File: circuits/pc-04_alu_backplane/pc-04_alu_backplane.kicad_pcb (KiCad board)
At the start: 2 copper layers, 99.1 x 99.1 mm, 16 parts, among them U1 74HC273, U2 74HC244, U3 74HC244, U4 74HC138, U5 4081, U6 4011, U7 4071, U8 74HC74, U9 4011

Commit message: Kicad upgrade to 9.0
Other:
- board text added: "ALU BACKPLANE PC-04 (REV. A)"
- board text removed: "ALU BACKPLANE PC-03 (REV. A)"

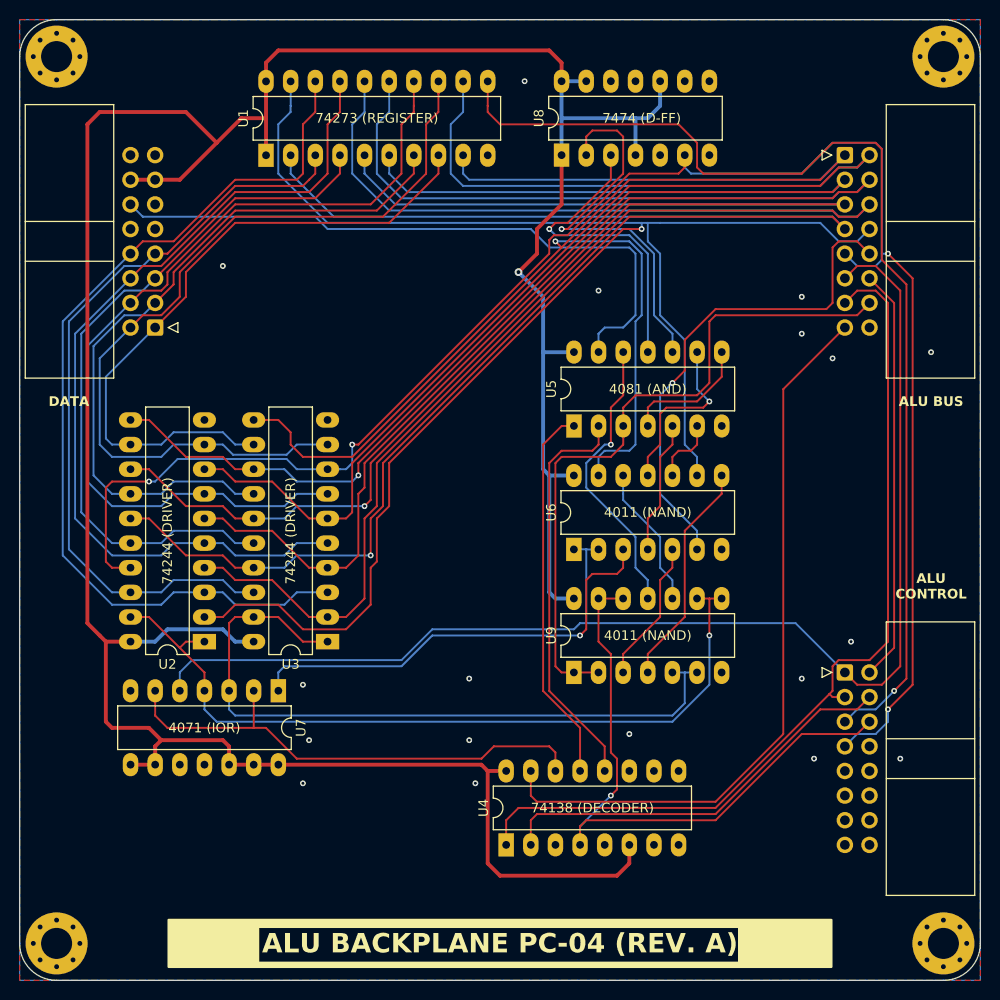
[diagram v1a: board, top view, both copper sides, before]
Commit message: pc-04: add missing pull-up resistors
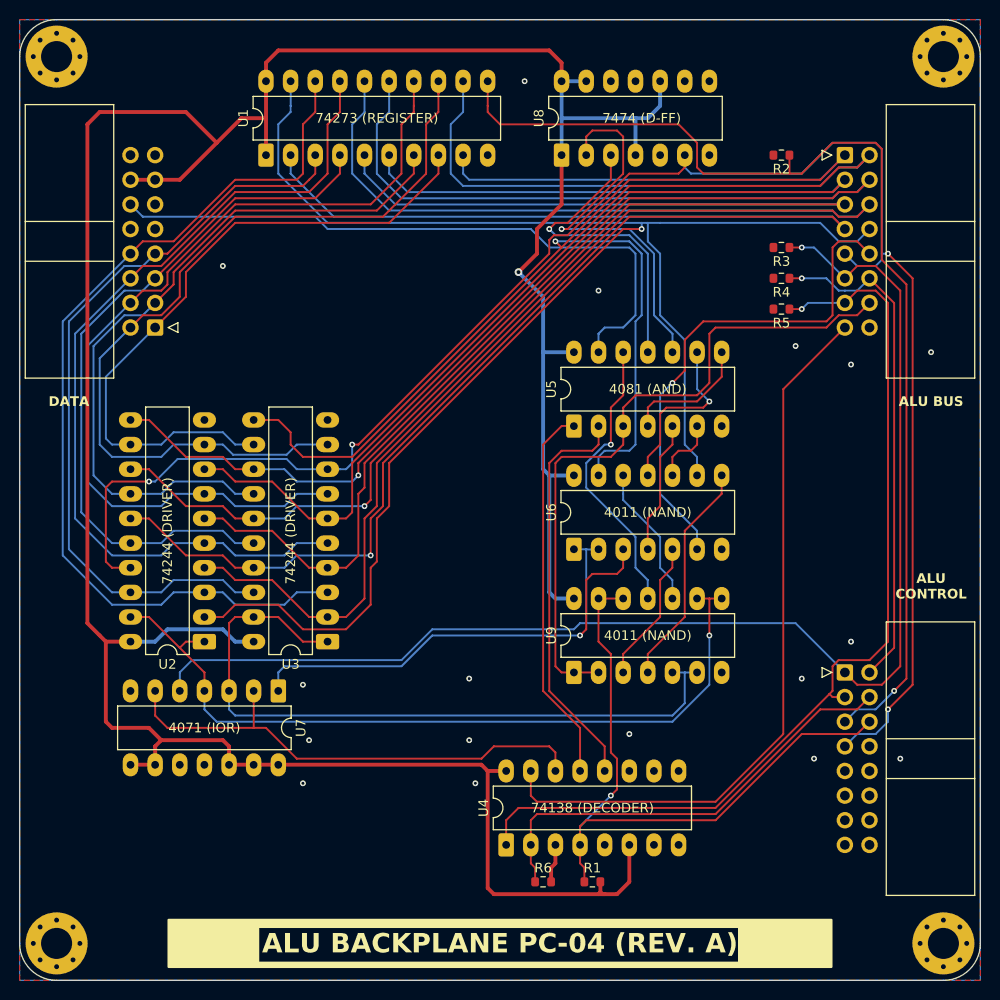
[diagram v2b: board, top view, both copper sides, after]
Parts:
- added R1: R, Resistor_SMD:R_0603_1608Metric, F.Cu at (99.7, 111.8)
- added R2: R, Resistor_SMD:R_0603_1608Metric, F.Cu at (119.2, 36.8)
- added R3: R, Resistor_SMD:R_0603_1608Metric, F.Cu at (119.2, 46.4)
- added R4: R, Resistor_SMD:R_0603_1608Metric, F.Cu at (119.2, 49.5)
- added R5: R, Resistor_SMD:R_0603_1608Metric, F.Cu at (119.2, 52.7)
- added R6: R, Resistor_SMD:R_0603_1608Metric, F.Cu at (94.6, 111.8)
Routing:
- net /cmd1: track 42.7 -> 52.1 mm, vias 0 -> 1
- net /cmd0: track 137.9 -> 144.9 mm, vias 0 -> 1
- net VCC: track 314.3 -> 320.4 mm
- net /cmd2: track 93.2 -> 99.2 mm, vias 0 -> 1
- net /~{readResult}: track 66.5 -> 70.5 mm
- net /cmd3: track 42.7 -> 46.7 mm
- net GND: track 0.00 -> 3.99 mm, vias 18 -> 17
- net /writeInput: track 113.4 -> 115.3 mm
- net /adder_carry_out: track 51.4 -> 52.1 mm
- net /~{adder_out}: track 70.8 -> 70.1 mm

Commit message: add filter and decoupling capacitors to all boards
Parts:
- added C1: C_Polarized, Capacitor_SMD:CP_Elec_5x5.3, F.Cu at (59.4, 32.8)
- added C2: C, Capacitor_SMD:C_0603_1608Metric, F.Cu at (62.1, 27.3)
- added C3: C, Capacitor_SMD:C_0603_1608Metric, F.Cu at (47.6, 88.9)
- added C4: C, Capacitor_SMD:C_0603_1608Metric, F.Cu at (85.7, 101.7)
- added C5: C, Capacitor_SMD:C_0603_1608Metric, F.Cu at (92.7, 58.6)
- added C6: C, Capacitor_SMD:C_0603_1608Metric, F.Cu at (92.7, 29.4)
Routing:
- net VCC: track 320.4 -> 335.0 mm
- net GND: vias 17 -> 23
